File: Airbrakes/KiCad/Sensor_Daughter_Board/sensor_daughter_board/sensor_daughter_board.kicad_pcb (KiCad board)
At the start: 2 copper layers, 28 x 12 mm, 11 parts, among them U1 BMI088, U2 BMP581, U3 BMM350

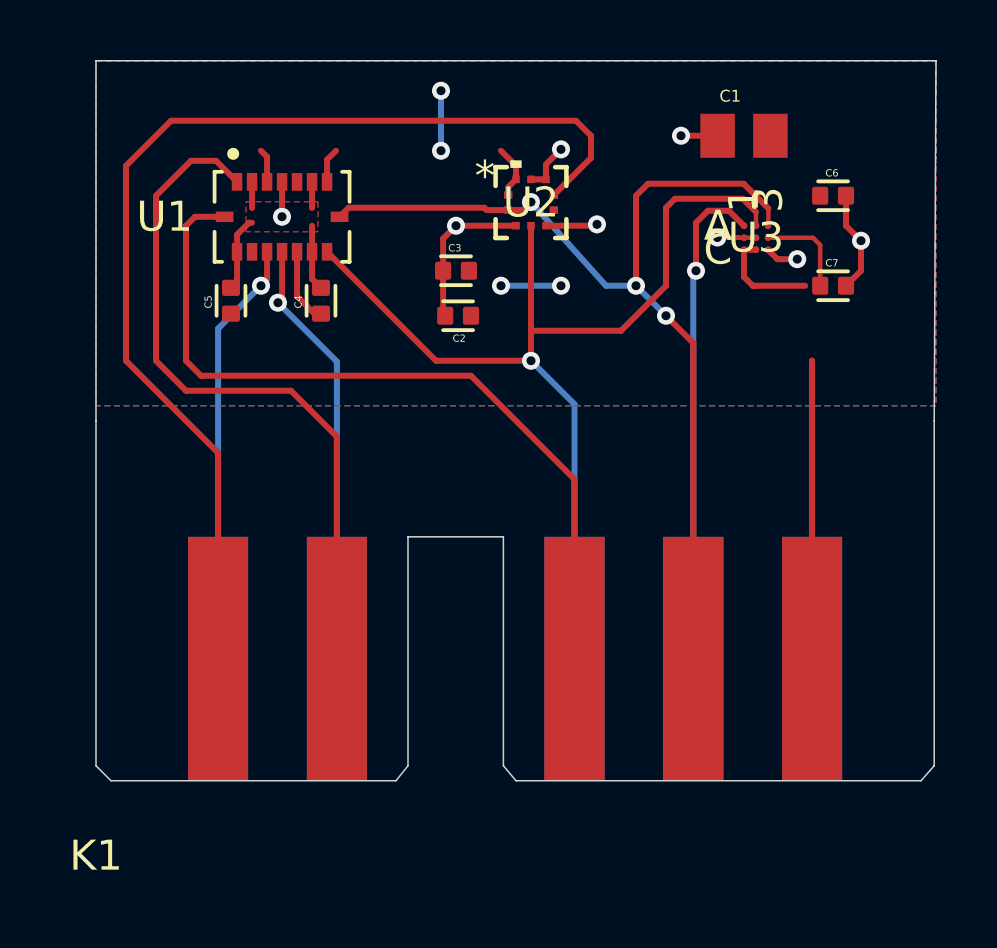
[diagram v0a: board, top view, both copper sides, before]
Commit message: make traces larger for PWR and GND
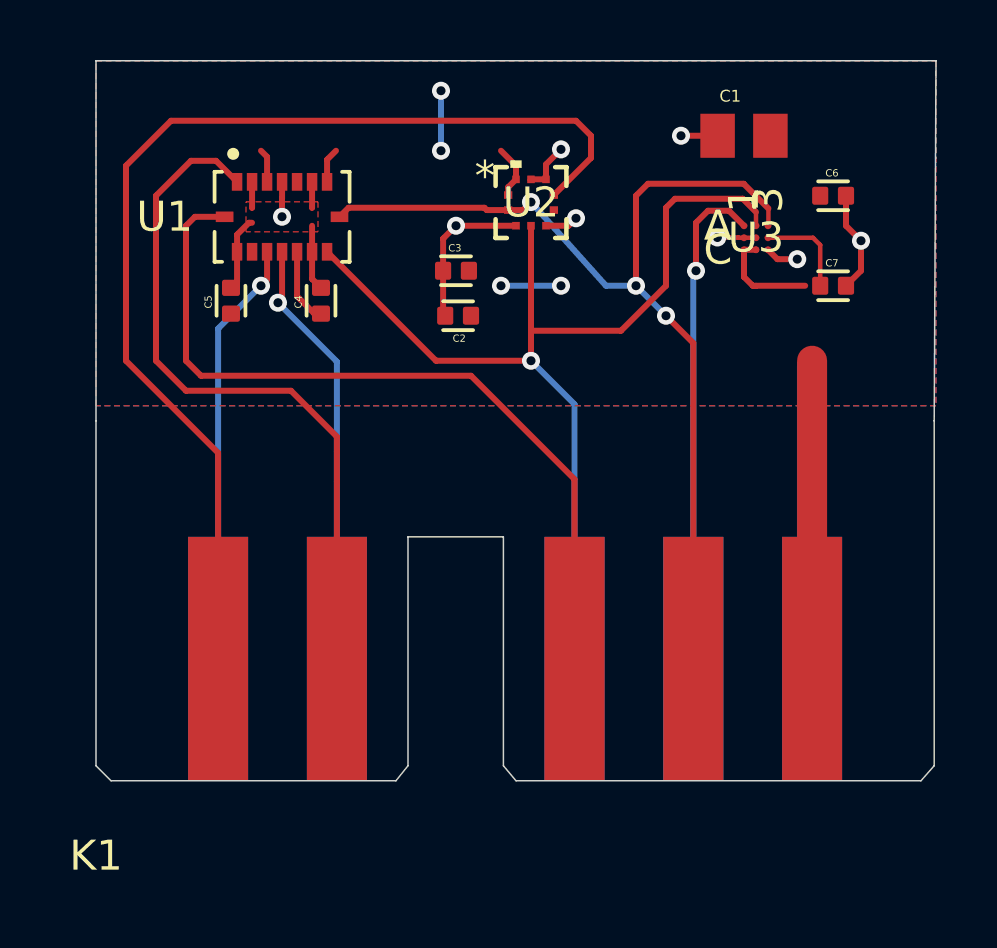
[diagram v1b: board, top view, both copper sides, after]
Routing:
- net GND: track 32.9 -> 32.3 mm
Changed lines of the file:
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@@
+	)
+	(segment
+		(start 111 42.25)
+		(end 110.75 42.5)
+		(width 0.2)
+		(layer "F.Cu")
+		(net 3)
 	)
 	(segment
@@
 	)
 	(segment
+		(start 110.75 42.5)
+		(end 109.999999 42.5)
+		(width 0.2)
+		(layer "F.Cu")
+		(net 3)
+	)
+	(segment
 		(start 120 42.5)
 		(end 120.5 43)
@@
 	)
 	(segment
-		(start 111.7 42.453998)
-		(end 111.653998 42.5)
-		(width 0.2)
-		(layer "F.Cu")
-		(net 3)
-	)
-	(segment
 		(start 116.40582 42.891779)
 		(end 116.414091 42.90005)
@@
 	)
 	(segment
-		(start 111.653998 42.5)
-		(end 109.999999 42.5)
-		(width 0.2)
-		(layer "F.Cu")
-		(net 3)
-	)
-	(segment
 		(start 100.2025 41.0375)
 		(end 100.2025 41.8975)
@@
 	)
 	(via
-		(at 111.7 42.453998)
+		(at 111 42.25)
 		(size 0.6)
 		(drill 0.3)
@@
 		(start 118.86608 54.613429)
 		(end 118.86608 47.174767)
-		(width 0.2)
+		(width 1)
 		(layer "B.Cu")
 		(net 3)
@@
 		(start 118.87 56.435)
 		(end 118.87 46.999125)
-		(width 0.2)
-		(layer "F.Cu")
-		(net 5)
+		(width 1)
+		(layer "F.Cu")
+		(net 5)
